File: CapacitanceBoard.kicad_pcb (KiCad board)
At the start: 2 copper layers, 17.4 x 25.3 mm, 15 parts, among them J1 Conn_01x04_Pin, J2 Conn_01x02_Pin, U1 AD7150BRMZ

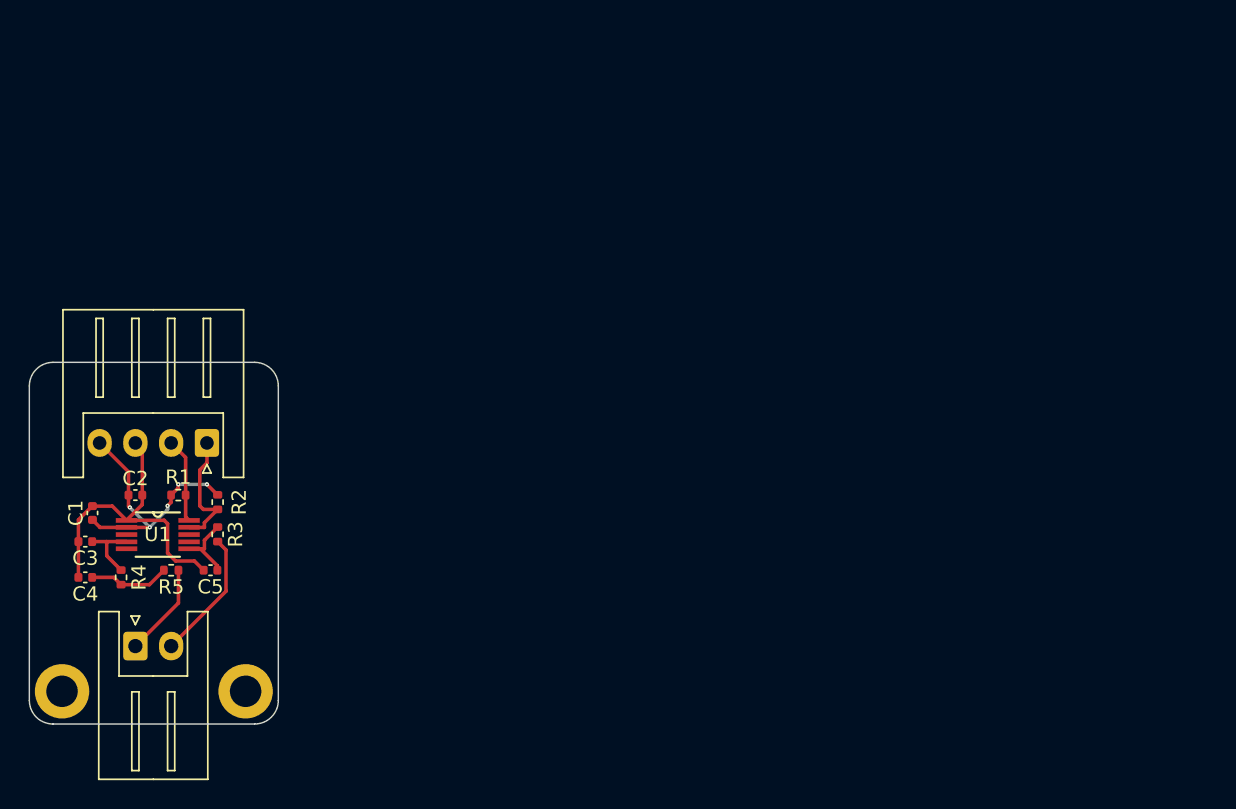
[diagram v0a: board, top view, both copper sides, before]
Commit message: Added Second Probe Input
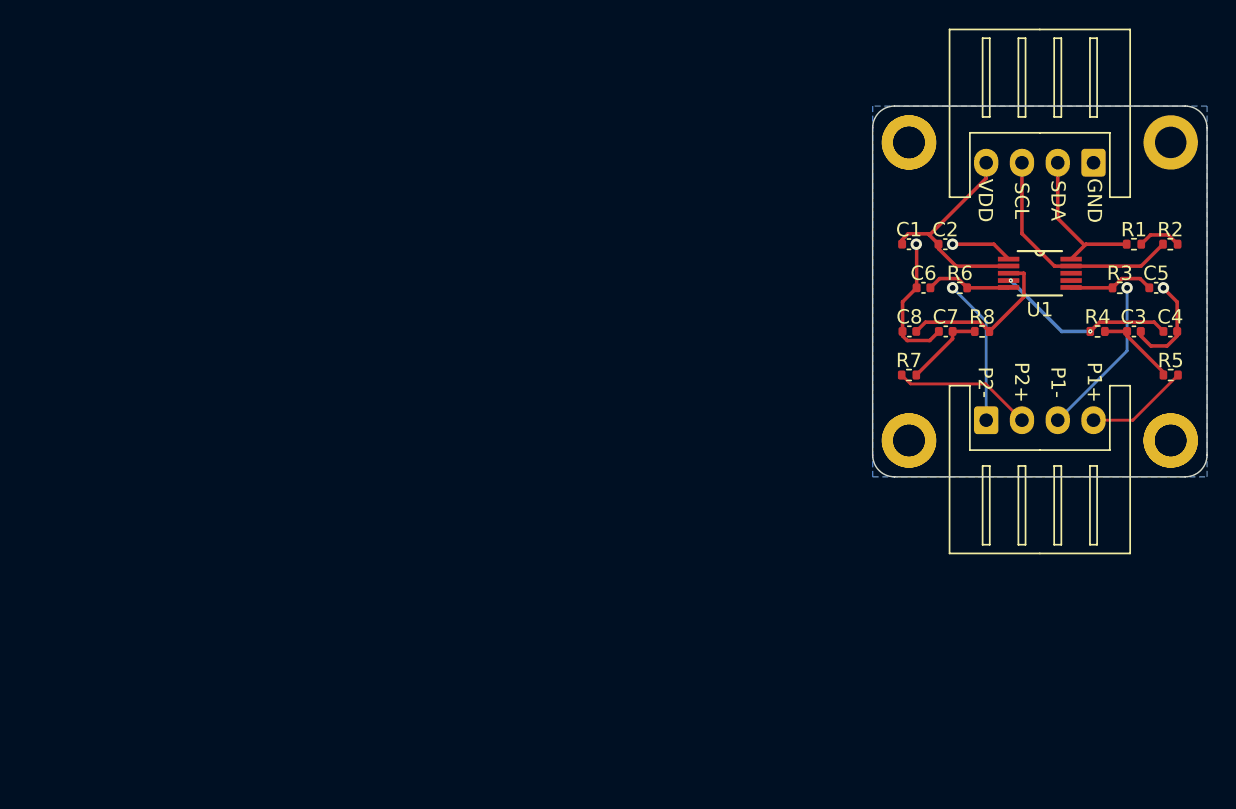
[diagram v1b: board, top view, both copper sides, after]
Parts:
- removed the ? at (119.1, 92.7)
- removed the REF** at (132.0, 92.7)
- added ?: , , F.Cu at (178.3, 75.2)
- added ?: , , F.Cu at (178.3, 54.4)
- added ?: , , F.Cu at (196.6, 75.2)
- added C6: 47p, Capacitor_SMD:C_0402_1005Metric, F.Cu at (179.3, 64.5)
- added C7: 68p, Capacitor_SMD:C_0402_1005Metric, F.Cu at (180.9, 67.6)
- added C8: 22p, Capacitor_SMD:C_0402_1005Metric, F.Cu at (178.3, 67.6)
- added G***: LOGO, iclr:iclr_logo_estd2018_10mm, B.Cu at (187.5, 64.8)
- added R6: 10k, Resistor_SMD:R_0402_1005Metric, F.Cu at (181.9, 64.5)
- added R7: 39k, Resistor_SMD:R_0402_1005Metric, F.Cu at (178.3, 70.6)
- added R8: 82k, Resistor_SMD:R_0402_1005Metric, F.Cu at (183.4, 67.6)
- added REF**: MountingHole_2.2mm_M2_DIN965_Pad, MountingHole:MountingHole_2.2mm_M2_DIN965_Pad, F.Cu at (196.6, 75.2)
- added REF**: MountingHole_2.2mm_M2_DIN965_Pad, MountingHole:MountingHole_2.2mm_M2_DIN965_Pad, F.Cu at (196.6, 54.4)
- added REF**: MountingHole_2.2mm_M2_DIN965_Pad, MountingHole:MountingHole_2.2mm_M2_DIN965_Pad, F.Cu at (178.3, 75.2)
- added REF**: MountingHole_2.2mm_M2_DIN965_Pad, MountingHole:MountingHole_2.2mm_M2_DIN965_Pad, F.Cu at (178.3, 54.4)
- C3: value 22p -> 68p
- C4: value 68p -> 22p
- J2: value Conn_01x02_Pin -> Conn_01x04_Pin; footprint Connector_JST:JST_XH_S2B-XH-A_1x02_P2.50mm_Horizontal -> Connector_JST:JST_XH_S4B-XH-A_1x04_P2.50mm_Horizontal
- moved C4 77.7 mm to (196.6, 67.6), turned to 0 degrees
- moved C3 74.7 mm to (194.0, 67.6), turned to 0 degrees
- moved R5 71.2 mm to (196.6, 70.6), turned to 0 degrees
- moved R4 70.4 mm to (191.5, 67.6), turned to 0 degrees
- moved R1 69.0 mm to (194.0, 61.5), turned to 0 degrees
- moved R2 69.0 mm to (196.6, 61.5), turned to 0 degrees
- moved C5 69.0 mm to (195.6, 64.5), turned to 0 degrees
- moved R3 65.4 mm to (193.0, 64.5), turned to 180 degrees
- moved J1 65.0 mm to (191.2, 55.8)
- moved U1 64.3 mm to (187.5, 63.5)
- moved J2 61.5 mm to (183.7, 73.8)
- moved C1 60.1 mm to (178.3, 61.5), turned to 0 degrees
- moved C2 59.3 mm to (180.8, 61.5)
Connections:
- C3 pad 1: /CIN1 -> Net-(C3-Pad1)
- C4 pad 1: Net-(C4-Pad1) -> /CIN1
- J1 pad 1: /SCL -> Earth
- J1 pad 2: /SDA -> SDA
- J1 pad 3: Earth -> SCL
- J2 pad 1: Net-(J2-Pin_1) -> Probe2-
- J2 pad 2: Net-(J2-Pin_2) -> Probe2+
- R3 pad 1: Probe- -> Probe1-
- R4 pad 1: Net-(C4-Pad1) -> /CIN1
- R4 pad 2: /CIN1 -> Net-(C3-Pad1)
- R5 pad 1: Net-(J2-Pin_1) -> Net-(C3-Pad1)
- R5 pad 2: Net-(C4-Pad1) -> Probe1+
- U1 pad 3: unconnected-(U1-CIN2-Pad3) -> /CIN2
- U1 pad 5: unconnected-(U1-EXC2-Pad5) -> /EXC2
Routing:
- net SCL: track 0.00 -> 16.4 mm
- net /CIN2: track 0.00 -> 11.8 mm
- net Probe1-: track 0.00 -> 11.3 mm, vias 0 -> 1
- net SDA: track 0.00 -> 10.9 mm
- net Probe2-: track 0.00 -> 10.2 mm, vias 0 -> 1
- net Probe2+: track 0.00 -> 9.71 mm
- net Net-(J2-Pin_2): track 9.13 -> 0.00 mm
- net /SCL: track 8.67 -> 0.00 mm
- net /CIN1: track 4.81 -> 12.7 mm, vias 0 -> 2
- net Probe1+: track 0.00 -> 7.21 mm
- net Net-(J2-Pin_1): track 6.55 -> 0.00 mm
- net /EXC2: track 0.00 -> 6.01 mm
- net /SDA: track 5.92 -> 0.00 mm
- net Net-(C3-Pad1): track 0.00 -> 5.65 mm
- net Net-(C7-Pad1): track 0.00 -> 5.65 mm
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- added copper zone on B.Cu, net Earth
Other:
- board size 17.4 x 25.3 mm -> 23.4 x 25.9 mm
- board text added: "Capacitive Fill Sensor Board"
- board text added: "GND"
- board text added: "P1+"
- board text added: "P1-"
- board text added: "P2+"
- board text added: "P2-"
- board text added: "SCL"
- board text added: "SDA"
- board text added: "VDD"
- board text removed: "Capacitive Fill Sensor"
